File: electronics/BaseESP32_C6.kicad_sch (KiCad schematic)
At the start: 13 parts, among them P3 CONN_01X09, P4 CONN_01X09, U7 ESP32-C6-MINI-1/U, Y1 Crystal

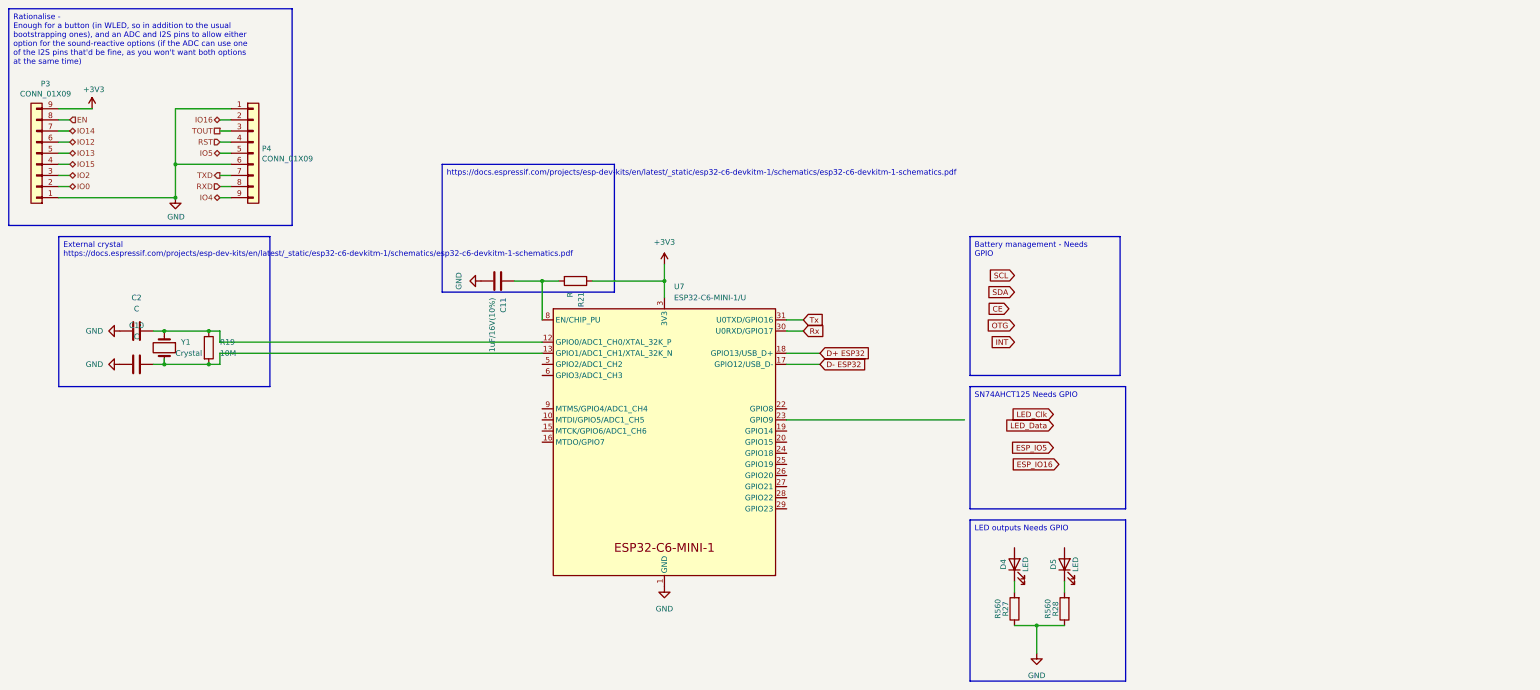
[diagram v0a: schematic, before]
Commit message: Connected esp pins, current battery protection using TI chip. check in before chip change
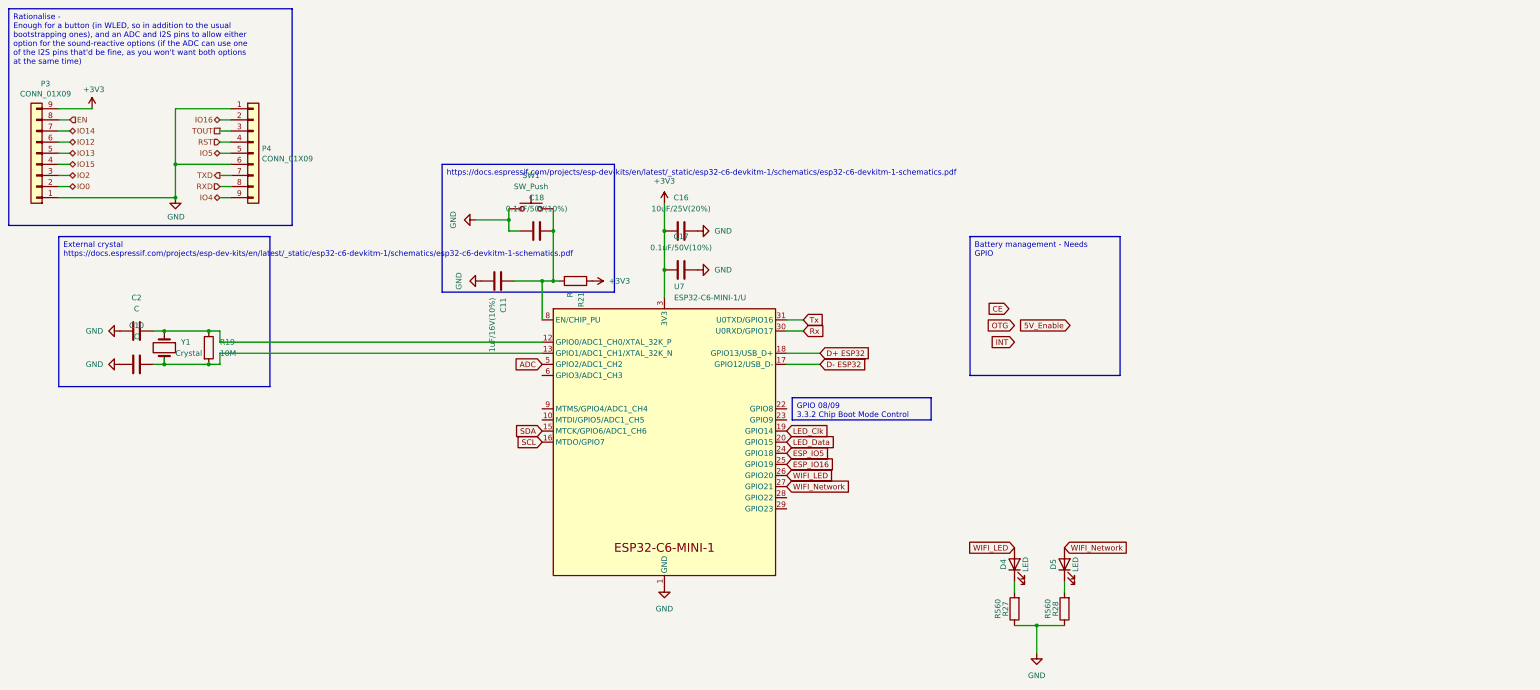
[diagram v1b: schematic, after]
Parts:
- added C16: 10uF/25V(20%), Capacitor_SMD:C_0603_1608Metric_Pad1.08x0.95mm_HandSolder, symbol Device:C
- added C17, C18: 0.1uF/50V(10%), Capacitor_SMD:C_0603_1608Metric_Pad1.08x0.95mm_HandSolder, symbol Device:C
- added SW1: SW_Push, Button_Switch_SMD:SW_Push_1P1T_NO_6x6mm_H9.5mm, symbol Switch:SW_Push
- C10, C11, C2: footprint (none) -> Capacitor_SMD:C_0603_1608Metric_Pad1.08x0.95mm_HandSolder
- R19, R21: footprint (none) -> Resistor_SMD:R_0603_1608Metric_Pad0.98x0.95mm_HandSolder
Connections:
- net +3V3: now also C16.2, C17.2
- net ESP_IO16: now also U7.25 (GPIO19)
- net ESP_IO5: now also U7.24 (GPIO18)
- net GND: now also C16.1, C17.1, C18.2, SW1.1
- net LED_Clk: now also U7.19 (GPIO14)
- net LED_Data: now also U7.20 (GPIO15)
- net SCL: now also U7.16 (MTDO/GPIO7)
- net SDA: now also U7.15 (MTCK/GPIO6/ADC1_CH6)
- net at C11.1, R21.2, U7.8 (EN/CHIP_PU): now also C18.1, SW1.2
- net WIFI_Network: now reaches D5.2 (A)
- net WIFI_Network: now also U7.27 (GPIO21)
- net WIFI_LED: now reaches D4.2 (A)
- net WIFI_LED: now also U7.26 (GPIO20)
- net ADC: now reaches U7.5 (GPIO2/ADC1_CH2)

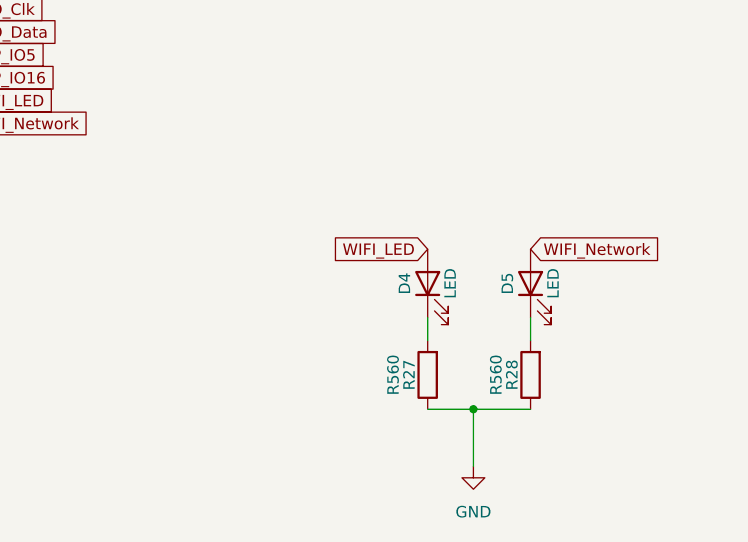
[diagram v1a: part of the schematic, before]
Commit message: Replaced batt management with IP5310, power switch still needed in schematic
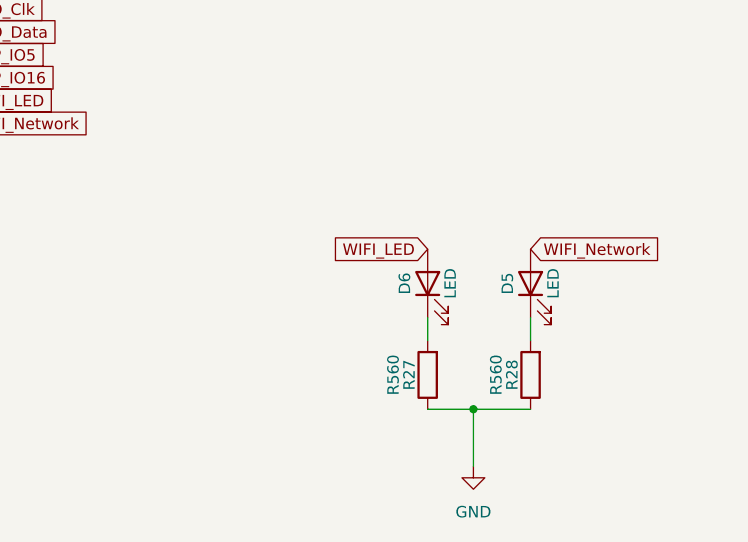
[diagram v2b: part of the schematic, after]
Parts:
- renumbered D4 to D6
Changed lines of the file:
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@@
   (symbol (lib_id "Device:LED") (at 250.19 137.16 90) (unit 1)
     (in_bom yes) (on_board yes) (dnp no)
-    (property "Reference" "D4" (at 247.65 137.16 0)
+    (property "Reference" "D6" (at 247.65 137.16 0)
       (effects (font (size 1.27 1.27)))
     )
@@
       (project "MyBikesGotLED"
         (path "/ea56fda8-6f8e-4826-a040-5c9b3e8e5cfa/88a3a1ef-5bc6-4f24-9217-01fd214eb76a"
-          (reference "D4") (unit 1)
+          (reference "D6") (unit 1)
         )
       )

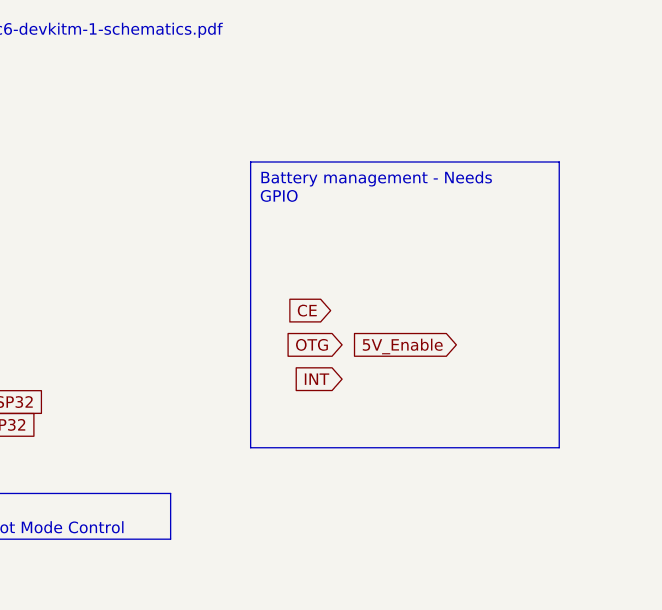
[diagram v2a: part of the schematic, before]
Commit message: Schematic complete except final pinouts for ESP and checking of swtich circuit and external crystal for ESP
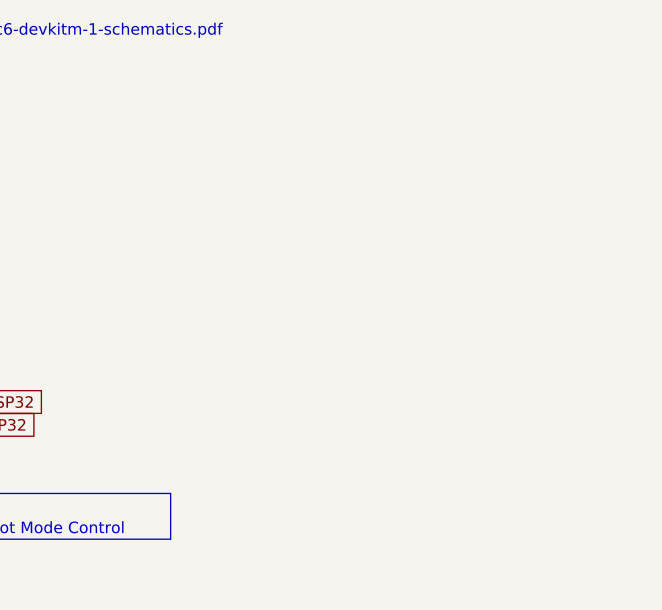
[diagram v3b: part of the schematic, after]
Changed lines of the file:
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@@
-    (effects (font (size 1.27 1.27)) (justify left top))
-  )
-  (text_box "Battery management - Needs GPIO"
-    (at 240.03 62.23 0) (size 34.29 31.75)
-    (stroke (width 0) (type default))
-    (fill (type none))
     (effects (font (size 1.27 1.27)) (justify left top))
   )
@@
     )
   )
-  (global_label "5V_Enable" (shape input) (at 262.89 82.55 180) (fields_autoplaced)
-    (effects (font (size 1.27 1.27)) (justify right))
-    (property "Intersheetrefs" "${INTERSHEET_REFS}" (at 30.48 15.24 0)
-      (effects (font (size 1.27 1.27)) hide)
-    )
-  )
   (global_label "D+ ESP32" (shape input) (at 205.74 88.9 0) (fields_autoplaced)
     (effects (font (size 1.27 1.27)) (justify left))
@@
     (property "Intersheetrefs" "${INTERSHEET_REFS}" (at 276.1068 133.35 0)
       (effects (font (size 1.27 1.27)) (justify left) hide)
-    )
-  )
-  (global_label "OTG" (shape input) (at 250.19 82.55 180) (fields_autoplaced)
-    (effects (font (size 1.27 1.27)) (justify right))
-    (property "Intersheetrefs" "${INTERSHEET_REFS}" (at 244.2909 82.55 0)
-      (effects (font (size 1.27 1.27)) (justify right) hide)
     )
   )
@@
     )
   )
-  (global_label "CE" (shape input) (at 248.92 78.74 180) (fields_autoplaced)
-    (effects (font (size 1.27 1.27)) (justify right))
-    (property "Intersheetrefs" "${INTERSHEET_REFS}" (at 244.17 78.74 0)
-      (effects (font (size 1.27 1.27)) (justify right) hide)
-    )
-  )
   (global_label "SCL" (shape input) (at 142.24 109.22 180) (fields_autoplaced)
     (effects (font (size 1.27 1.27)) (justify right))
@@
     )
   )
-  (global_label "INT" (shape input) (at 250.19 86.36 180) (fields_autoplaced)
-    (effects (font (size 1.27 1.27)) (justify right))
-    (property "Intersheetrefs" "${INTERSHEET_REFS}" (at 244.9561 86.36 0)
-      (effects (font (size 1.27 1.27)) (justify right) hide)
-    )
-  )

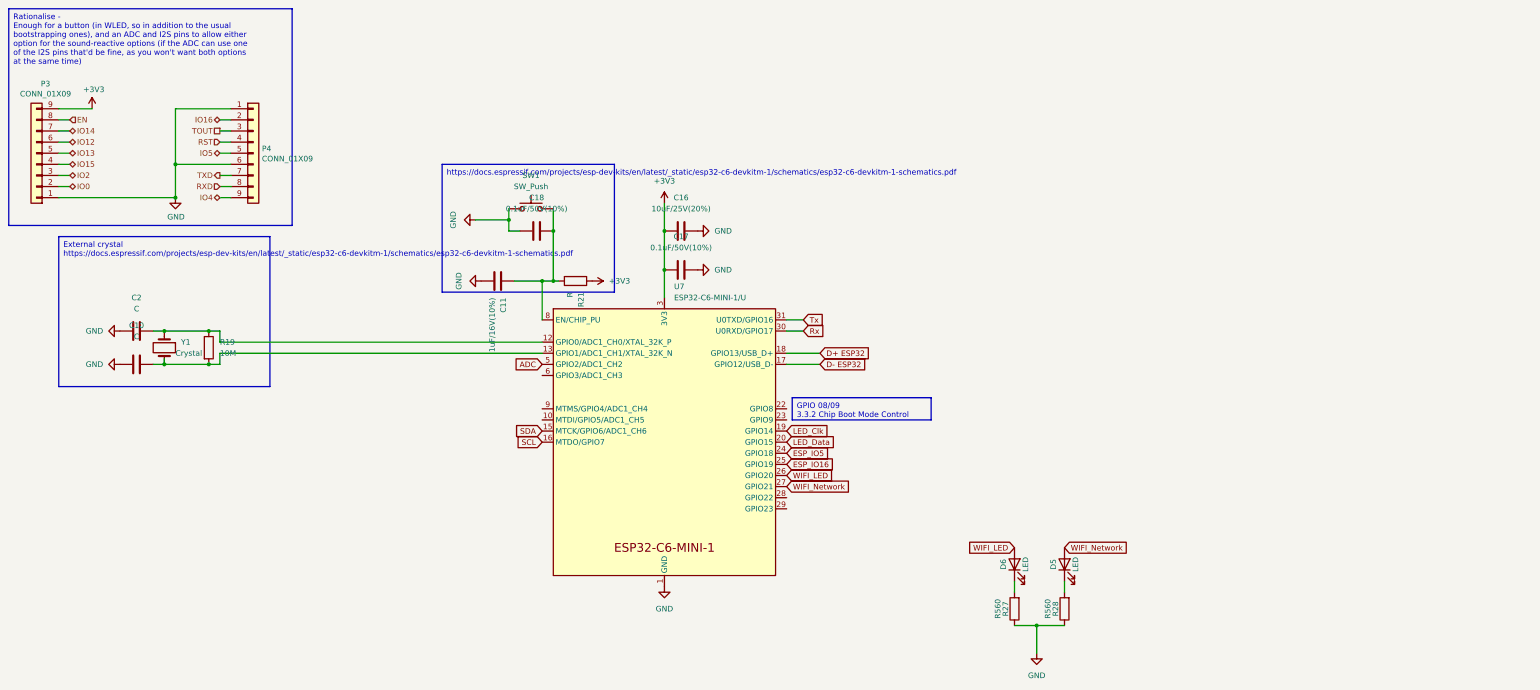
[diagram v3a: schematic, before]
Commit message: Tracks placed, DRC passess excpept silkscreen. Needs BOM before fabrication
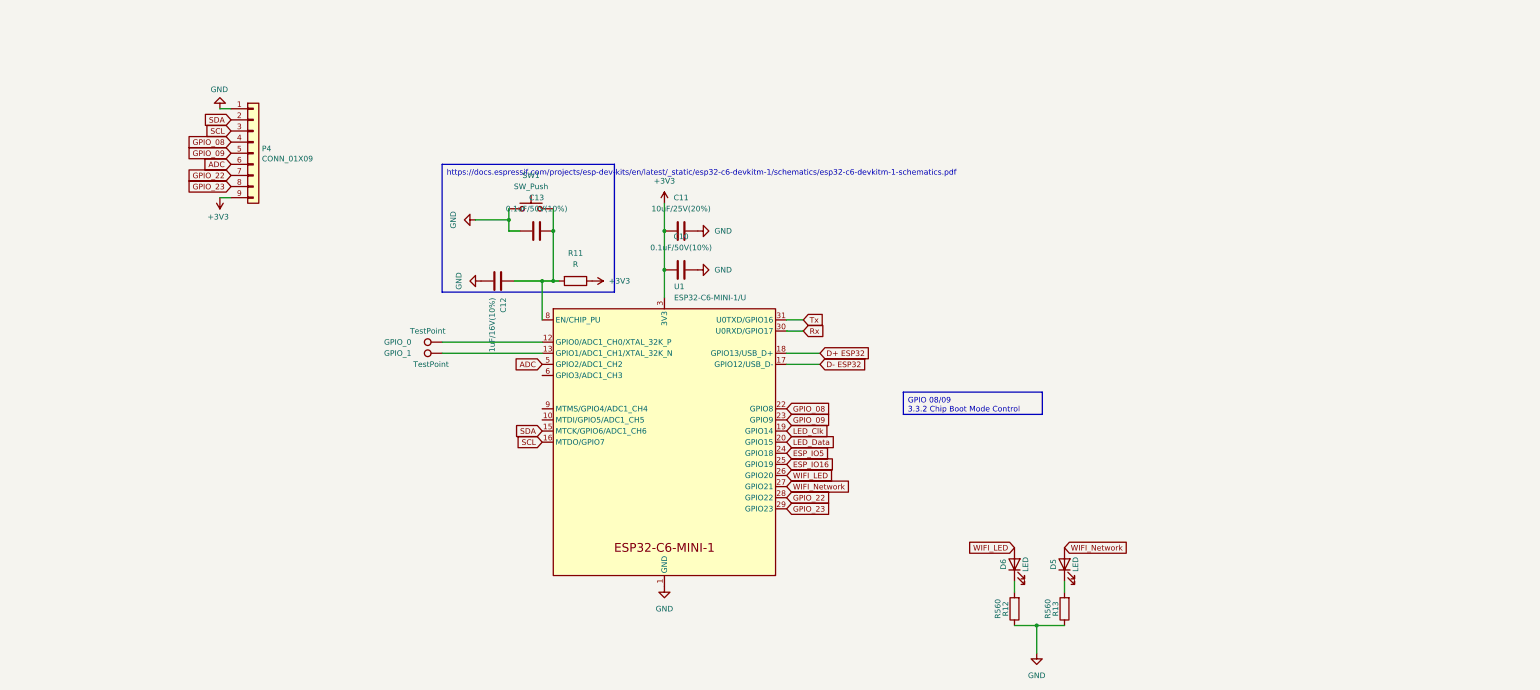
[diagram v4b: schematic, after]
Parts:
- removed C10, C2: C, Capacitor_SMD:C_0603_1608Metric_Pad1.08x0.95mm_HandSolder, symbol Device:C
- removed P3: CONN_01X09, Connector_PinSocket_2.54mm:PinSocket_1x09_P2.54mm_Vertical, symbol Connector_Generic:Conn_01x09
- removed R19: 10M, Resistor_SMD:R_0603_1608Metric_Pad0.98x0.95mm_HandSolder, symbol Device:R
- removed Y1: Crystal, symbol Device:Crystal
- added GPIO_0, GPIO_1: TestPoint, TestPoint:TestPoint_Pad_D2.5mm, symbol Connector:TestPoint
- renumbered C17 to C10, C16 to C11, C11 to C12, C18 to C13, R21 to R11, R27 to R12, R28 to R13, U7 to U1
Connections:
- net IO16 is gone; now on net SDA: P4.2 (Pin_2)
- net IO4 is gone; now on net +3V3: P4.9 (Pin_9)
- net IO5 is gone; now on net GPIO_09: P4.5 (Pin_5)
- net RST is gone; now on net GPIO_08: P4.4 (Pin_4)
- net RXD is gone; now on net GPIO_23: P4.8 (Pin_8)
- net TOUT is gone; now on net SCL: P4.3 (Pin_3)
- net TXD is gone; now on net GPIO_22: P4.7 (Pin_7)
- net ADC: now also P4.6 (Pin_6)
- net GND: no longer P4.6 (Pin_6)
- net at U1.12 (GPIO0/ADC1_CH0/XTAL_32K_P): now also GPIO_0.1
- net at U1.13 (GPIO1/ADC1_CH1/XTAL_32K_N): now also GPIO_1.1
- net GPIO_08: now reaches U1.22 (GPIO8)
- net GPIO_09: now reaches U1.23 (GPIO9)
- net GPIO_22: now reaches U1.28 (GPIO22)
- net GPIO_23: now reaches U1.29 (GPIO23)

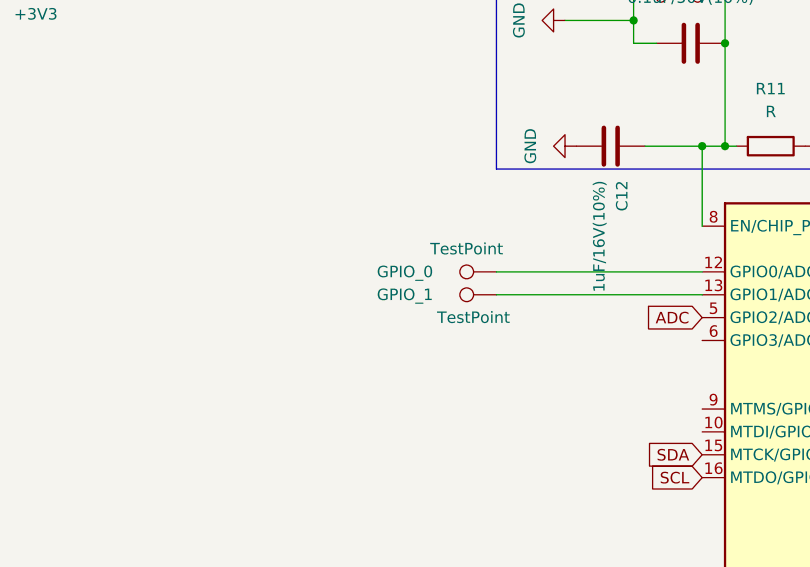
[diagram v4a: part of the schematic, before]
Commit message: Fixed ground planes, tidied silkscreen, added keepout zone for ESP
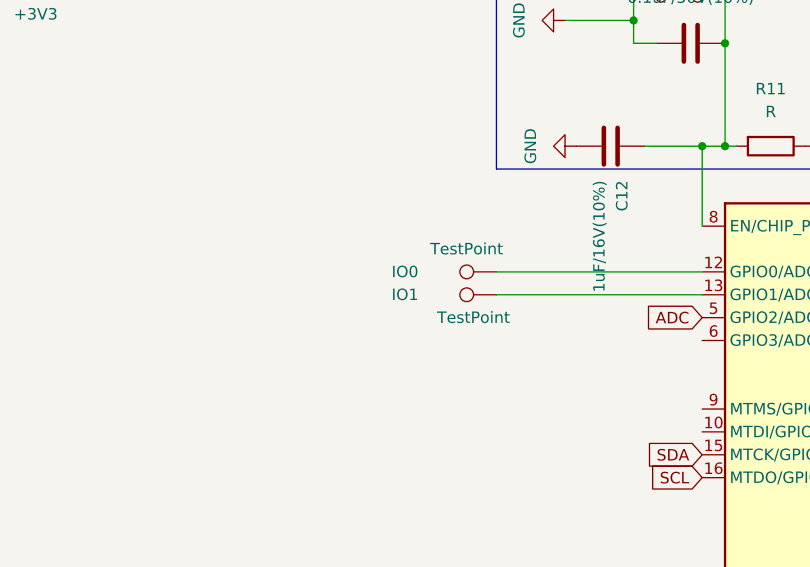
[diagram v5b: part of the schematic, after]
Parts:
- renumbered GPIO_0 to IO0, GPIO_1 to IO1
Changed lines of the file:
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@@
   (symbol (lib_id "Connector:TestPoint") (at 119.38 88.9 90) (unit 1)
     (in_bom yes) (on_board yes) (dnp no)
-    (property "Reference" "GPIO_1" (at 109.22 88.9 90)
+    (property "Reference" "IO1" (at 109.22 88.9 90)
       (effects (font (size 1.27 1.27)))
     )
@@
       (project "MyBikesGotLED"
         (path "/ea56fda8-6f8e-4826-a040-5c9b3e8e5cfa/88a3a1ef-5bc6-4f24-9217-01fd214eb76a"
-          (reference "GPIO_1") (unit 1)
+          (reference "IO1") (unit 1)
         )
       )
@@
   (symbol (lib_id "Connector:TestPoint") (at 119.38 86.36 90) (unit 1)
     (in_bom yes) (on_board yes) (dnp no)
-    (property "Reference" "GPIO_0" (at 109.22 86.36 90)
+    (property "Reference" "IO0" (at 109.22 86.36 90)
       (effects (font (size 1.27 1.27)))
     )
@@
       (project "MyBikesGotLED"
         (path "/ea56fda8-6f8e-4826-a040-5c9b3e8e5cfa/88a3a1ef-5bc6-4f24-9217-01fd214eb76a"
-          (reference "GPIO_0") (unit 1)
+          (reference "IO0") (unit 1)
         )
       )
